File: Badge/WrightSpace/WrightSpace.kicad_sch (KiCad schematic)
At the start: 28 parts, among them J1 Conn_01x02, J2 Conn_01x02, J3 10118193-0001LF, J4 Conn_02x03_Counter_Clockwise, J5 Conn_02x03_Counter_Clockwise, J6 Conn_02x03_Counter_Clockwise, Q1 BC817, Q2 BC817, SW1 SW_SPDT, SW2 SW_SPDT, SW3 SW_SPDT, SW4 SW_SPDT, U1 ESP32-S2-SOLO, U2 HT75xx-1-SOT89

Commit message: an evenings updates
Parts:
- removed J1, J2: Conn_01x02, aerospace_badge:motor_connector, symbol Connector_Generic:Conn_01x02
- removed Q1, Q2: BC817, Package_TO_SOT_SMD:SOT-23, symbol Transistor_BJT:BC817
- removed R1: 1K, Resistor_SMD:R_0805_2012Metric_Pad1.20x1.40mm_HandSolder, symbol Device:R
- removed SW2, SW3: SW_SPDT, aerospace_badge:switch_JS202011SCQN, symbol Switch:SW_SPDT
- added D2, D3, D4, D5, D6: LED, LED_SMD:LED_1206_3216Metric_ReverseMount_Hole1.8x2.4mm, symbol Device:LED
- added R6, R7: 330, Resistor_SMD:R_0805_2012Metric_Pad1.20x1.40mm_HandSolder, symbol Device:R
- C2: value 1uF -> 100pF
- C3: value 10uF -> 1uF
- D1: footprint sunled:XZDGK45WT-9 -> LED_SMD:LED_1206_3216Metric_ReverseMount_Hole1.8x2.4mm
- R3, R4, R5: value 1K -> 330
- renumbered J5 to J1, J6 to J2, R2 to R1, R8 to R10, R9 to R2, R6 to R8, R7 to R9, SW4 to SW2
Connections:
- net Boot_Button: now also J4.5 (Pin_5); no longer J4.6 (Pin_6)
- net EN: now also J4.6 (Pin_6); no longer J4.5 (Pin_5)
- net GND: now also R3.2, R4.2, R5.2, R6.2, R7.2
- net VBUS: no longer R3.1, R4.2
- net at R5.1: now also D4.1 (K)
- net at R4.1: now also D3.1 (K)
- net LED6: now reaches U1.10 (GPIO17/U1TXD/ADC2_CH6/DAC_1)
- net LED6: now also D6.2 (A)
- net LED2: now reaches U1.21 (GPIO13/TOUCH13/ADC2_CH2/FSPIQ/FSPIIO7)
- net LED2: now also D2.2 (A)
- net LED3: now reaches U1.22 (GPIO14/TOUCH14/ADC2_CH3/FSPIWP/FSPIDQS)
- net LED3: now also D3.2 (A)
- net LED4: now reaches U1.8 (GPIO15/U0RTS/ADC2_CH4/XTAL_32K_P)
- net LED4: now also D4.2 (A)
- net LED5: now reaches U1.9 (GPIO16/U0CTS/ADC2_CH5/XTAL_32K_N)
- net LED5: now also D5.2 (A)
- net MOTOR_CTRL_MCU: no longer names the net of U1.16 (GPIO46)
- net MOTOR_CTRL_MCU_BACKUP: no longer names the net of U1.35 (MTMS/GPIO42)
- new net: D5.1 (K), R6.1
- new net: D2.1 (K), R3.1
- new net: D6.1 (K), R7.1
- no-connect marks 24 -> 21
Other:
- note added: "Programming Interface"
- note added: "The Reset (Enable) and Boot Buttons can be externalized to simplify fabrication. This will then require a rig to be assembled for programming purposes."
- note removed: "Boot Button"
- note removed: "MCU or Override Switch WiFi Controlled"
- note removed: "Manual Rotor Power Switch"
- note removed: "Motor Control"
- note removed: "Programming Connection"
- note removed: "Reset Button"
- note removed: "This needs to be here to ensure the propellers aren't spinner full speed while in backup mode. Alternatively, the other side of the backup switch could serve to go full speed/unregulated."
- moved on the sheet: D1, J1, J2, R1, R2, SW1

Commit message: weekend updates to Wright Stuff
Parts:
- removed J3: 10118193-0001LF, 10118193-0001LF:AMPHENOL_10118193-0001LF, symbol 10118193-0001LF:10118193-0001LF
- removed U2: HT75xx-1-SOT89, Package_TO_SOT_SMD:SOT-89-3, symbol Regulator_Linear:HT75xx-1-SOT89
- added C4, C5: 10uF, symbol Device:C
- added D7, D8: SunLED_RGB_ReverseMount, LED_SMD:LED_Kingbright_APFA3010_3x1.5mm_Horizontal, symbol LED:SunLED_RGB_ReverseMount
- added J2: ~, Badge_Libraries:Wright X2, symbol WrightStuff:WrightStuff
- added R1, R10, R11, R2: 30, symbol Device:R
- added R12, R13: 150, symbol Device:R
- added U2: ~, Package_TO_SOT_SMD:SOT-89-5, symbol av_Badge2023:R1170H331B-T1-FE
- J1: renamed from J4; footprint Connector_PinSocket_2.54mm:PinSocket_2x03_P2.54mm_Vertical -> aerospace_badge:esp32_programming_connector
- J3: renamed from J1; footprint Connector_PinSocket_2.54mm:PinSocket_2x03_P2.54mm_Vertical -> aerospace_badge:sao_1.69
- J4: renamed from J2; footprint Connector_PinSocket_2.54mm:PinSocket_2x03_P2.54mm_Vertical -> aerospace_badge:sao_1.69
- renumbered R9 to R14, R10 to R15, R8 to R16, R1 to R3, R2 to R4, R3 to R5, R4 to R6, R5 to R7, R6 to R8, R7 to R9
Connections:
- net VUSB is gone; now on net VBUS: SW2.1 (A)
- net EN: now also R16.1; no longer R16.2
- net GND: now also C4.1, C5.2, U2.2 (GND)
- net LED1: now also U1.13 (GPIO19/U1RTS/ADC2_CH8/CLK_OUT2/USB_D-); no longer U1.20 (GPIO12/TOUCH12/ADC2_CH1/FSPICLK/FSPIIO6)
- net LED2: now also U1.14 (GPIO20/U1CTS/ADC2_CH9/CLK_OUT1/USB_D+); no longer U1.21 (GPIO13/TOUCH13/ADC2_CH2/FSPIQ/FSPIIO7)
- net LED3: now also U1.23 (GPIO21); no longer U1.22 (GPIO14/TOUCH14/ADC2_CH3/FSPIWP/FSPIDQS)
- net LED4: now also U1.24 (SPIIO4/GPIO33/FSPIHD); no longer U1.8 (GPIO15/U0RTS/ADC2_CH4/XTAL_32K_P)
- net LED5: now also U1.25 (SPIIO5/GPIO34/FSPICS0); no longer U1.9 (GPIO16/U0CTS/ADC2_CH5/XTAL_32K_N)
- net LED6: now also U1.28 (SPIIO6/GPIO35/FSPID); no longer U1.10 (GPIO17/U1TXD/ADC2_CH6/DAC_1)
- net VBUS: now also BT1.1 (+), C4.2, U2.4 (Vin); no longer SW2.2 (B)
- net VDD33: now also R16.2, C5.1, D7.2 (A), D8.2 (A), U2.5 (Vout); no longer R16.1
- net WiFi_On/Off: now also R3.2, U1.11 (GPIO18/U1RXD/ADC2_CH7/DAC_2/CLK_OUT3); no longer U1.26 (GPIO45)
- net at SW2.3 (C): no longer BT1.1 (+)
- net at SW1.1 (A): no longer R3.2
- net TX: now reaches J1.1 (Pin_1), U1.37 (U0TXD/GPIO43/CLK_OUT1)
- net RX: now reaches J1.2 (Pin_2), U1.36 (U0RXD/GPIO44/CLK_OUT2)
- net Touch3: now reaches U1.15 (GPIO3/TOUCH3/ADC1_CH2)
- net Touch3: now also J2.3 (Touch3)
- net Touch2: now reaches U1.38 (GPIO2/TOUCH2/ADC1_CH1)
- net Touch2: now also J2.2 (Touch2)
- net Touch1: now reaches U1.39 (GPIO1/TOUCH1/ADC1_CH0)
- net Touch1: now also J2.1 (Touch1)
- net Touch4: now reaches U1.4 (GPIO4/TOUCH4/ADC1_CH3)
- net Touch4: now also J2.4 (Touch4)
- net Touch5: now reaches U1.5 (GPIO5/TOUCH5/ADC1_CH4)
- net Touch5: now also J2.5 (Touch5)
- net Touch6: now reaches U1.6 (GPIO6/TOUCH6/ADC1_CH5)
- net Touch6: now also J2.6 (Touch6)
- new net: D8.3 (G), R11.2
- new net: D8.4 (B), R2.2
- new net: SW2.2 (B), U2.1 (CE)
- new net: D7.3 (G), R10.2
- new net: D7.1 (R), R12.2
- new net: D7.4 (B), R1.2
- new net: D8.1 (R), R13.2
- new net LED1_B: R1.1, U1.22 (GPIO14/TOUCH14/ADC2_CH3/FSPIWP/FSPIDQS)
- new net LED1_G: R10.1, U1.21 (GPIO13/TOUCH13/ADC2_CH2/FSPIQ/FSPIIO7)
- new net LED1_R: R12.1, U1.20 (GPIO12/TOUCH12/ADC2_CH1/FSPICLK/FSPIIO6)
- new net LED2_B: R2.1, U1.10 (GPIO17/U1TXD/ADC2_CH6/DAC_1)
- new net LED2_G: R11.1, U1.9 (GPIO16/U0CTS/ADC2_CH5/XTAL_32K_N)
- new net LED2_R: R13.1, U1.8 (GPIO15/U0RTS/ADC2_CH4/XTAL_32K_P)
- no-connect marks 21 -> 13
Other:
- note added: "3 AAA Batteries Nominal 4.5V decaying"
- note added: "Touch Points"
- note added: "WiFi On/Off Switch"
- note removed: "GND"
- note removed: "RX"
- note removed: "TX"
- note removed: "WiFi Switch"
- title: 2023 Badge for AV Def Con -> Wright Stuff 
- moved on the sheet: BT1, C1, D1, D2, D3, D4, D5, D6, J1, J3, J4, R14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

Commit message: updated schematics
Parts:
- C1, C3: MPN (none) -> CL21B105KAFNNNE
- C2: value 100pF -> 10uF; MPN (none) -> TCP0J106M8R
- C4, C5: footprint (none) -> Capacitor_SMD:C_0805_2012Metric_Pad1.18x1.45mm_HandSolder; MPN (none) -> TCP0J106M8R
- D7, D8: MPN (none) -> XZMDKCBDDG45S-9
- R1, R10, R11, R2: footprint (none) -> Resistor_SMD:R_0805_2012Metric; MPN (none) -> RC0805FR-0730RL
- R12, R13: footprint (none) -> Resistor_SMD:R_0805_2012Metric; MPN (none) -> RC0805JR-07150RL
- U1: MPN (none) -> ESP32-S2-SOLO-2-N4
- U2: MPN (none) -> R1170H331B-T1-FE
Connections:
- net GND: now also C5.1; no longer C5.2
- net VDD33: now also C5.2; no longer C5.1
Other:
- note added: "Touch Ideas (all silver): - Ropp Signature - Small Circle on Back of Satellite - Small Circle on lower part of Satellite - Satellite Dish outer - Satellite Dish Inner"

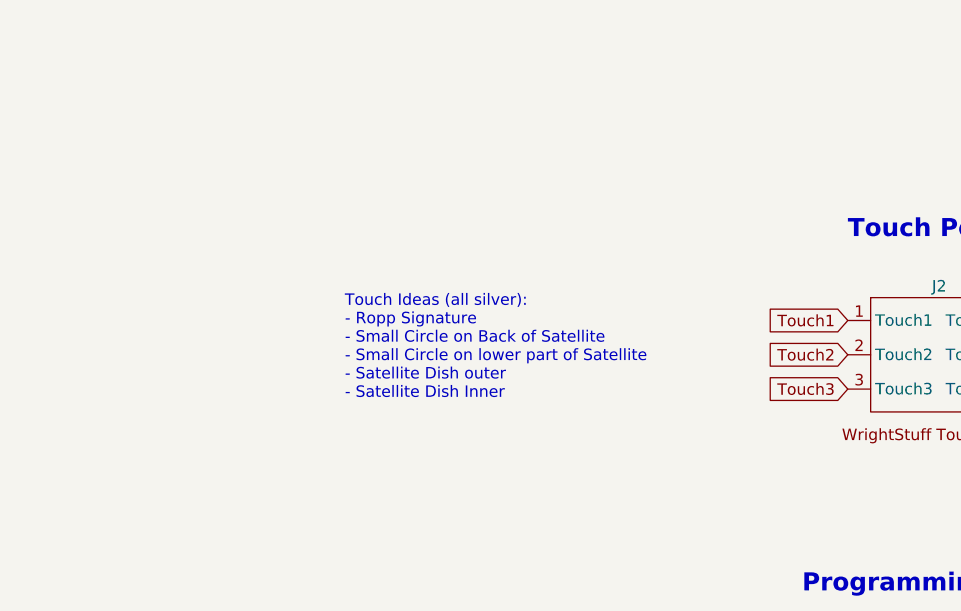
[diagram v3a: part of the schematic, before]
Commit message: updated footprint for linear voltage regulator on both badges
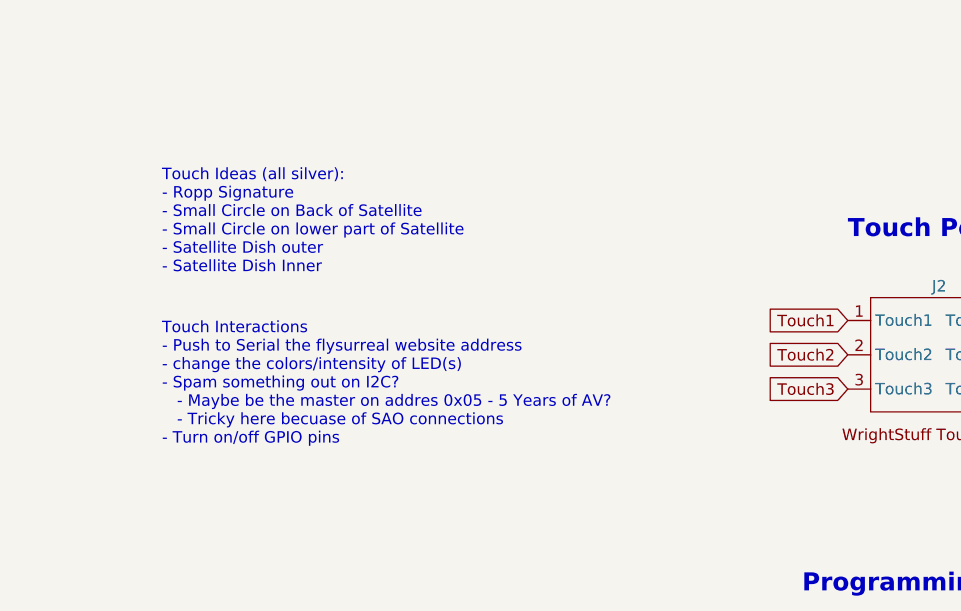
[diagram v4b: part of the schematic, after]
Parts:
- U2: footprint Package_TO_SOT_SMD:SOT-89-5 -> aerospace_badge:R1170X-SOT-89-5
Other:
- note added: "Touch Interactions - Push to Serial the flysurreal website address - change the colors/intensity of LED(s) - Spam something out on I2C? - Maybe be the master on addres 0x05 - 5 Years of AV? - Tricky here becuase of SAO connections - Turn on/off GPIO pins"
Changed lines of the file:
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@@
     (effects (font (size 2 2) (thickness 0.4) bold) (justify left bottom))
+  )
+  (text "Touch Interactions\n- Push to Serial the flysurreal website address\n- change the colors/intensity of LED(s)\n- Spam something out on I2C?\n   - Maybe be the master on addres 0x05 - 5 Years of AV?\n   - Tricky here becuase of SAO connections\n- Turn on/off GPIO pins\n"
+    (at 304.8 139.7 0)
+    (effects (font (size 1.27 1.27)) (justify left bottom))
   )
   (text "3 AAA Batteries\nNominal 4.5V decaying" (at 304.8 49.53 0)
@@
   )
   (text "Touch Ideas (all silver):\n- Ropp Signature\n- Small Circle on Back of Satellite\n- Small Circle on lower part of Satellite\n- Satellite Dish outer\n- Satellite Dish Inner"
-    (at 325.12 134.62 0)
+    (at 304.8 120.65 0)
     (effects (font (size 1.27 1.27)) (justify left bottom))
   )
@@
       (effects (font (size 1.27 1.27)))
     )
-    (property "Footprint" "Package_TO_SOT_SMD:SOT-89-5" (at 356.87 38.1 0)
-      (effects (font (size 1.27 1.27)) hide)
-    )
+    (property "Footprint" "aerospace_badge:R1170X-SOT-89-5" (at 356.87 38.1 0)
+      (effects (font (size 1.27 1.27)) hide)
+    )

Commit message: refined artwork and poc WrightStuff
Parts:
- removed J3, J4: Conn_02x03_Counter_Clockwise, aerospace_badge:sao_1.69, symbol Connector_Generic:Conn_02x03_Counter_Clockwise
- added J3, J4: ~, aerospace_badge:sao_1.69, symbol av_Badge2023:SAO_v1.69
- J2: footprint Badge_Libraries:Wright X2 -> Badge_Libraries:Wright X3
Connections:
- net GND: now also J3.2 (GND), J4.2 (GND)
- net GPIO1: now also J3.5 (GPIO1), J4.5 (GPIO1)
- net GPIO2: now also J3.6 (GPIO2), J4.6 (GPIO2)
- net SCL: now also J3.4 (SCL), J4.4 (SCL)
- net SDA: now also J3.3 (SDA), J4.3 (SDA)
- net VDD33: now also J3.1 (Vcc), J4.1 (Vcc)

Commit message: artwork tweaks to get more into KiCad
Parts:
- D1, D2, D3, D4, D5, D6: footprint LED_SMD:LED_1206_3216Metric_ReverseMount_Hole1.8x2.4mm -> aerospace_badge:led_in-s124ar; MPN (none) -> IN-S124ARUW
- D7, D8: footprint LED_SMD:LED_Kingbright_APFA3010_3x1.5mm_Horizontal -> sunled:XZMDKCBDDG45S-9

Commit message: updates, prior to fabrication
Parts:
- removed D8: SunLED_RGB_ReverseMount, sunled:XZMDKCBDDG45S-9, symbol LED:SunLED_RGB_ReverseMount
- removed J4: ~, aerospace_badge:sao_1.69, symbol av_Badge2023:SAO_v1.69
- added D1, D2, D4, D5: SunLED_RGB_ReverseMount, sunled:XZMDKCBDDG45S-9, symbol LED:SunLED_RGB_ReverseMount
- added R1, R10, R4, R5, R7, R8: 30, Resistor_SMD:R_0805_2012Metric, symbol Device:R
- added R12, R15, R16: 150, Resistor_SMD:R_0805_2012Metric, symbol Device:R
- renumbered D5 to D10, D6 to D11, D7 to D3, D1 to D6, D2 to D7, D3 to D8, D4 to D9, R12 to R14, R4 to R17, R5 to R18, R6 to R19, R7 to R20, R8 to R21, R9 to R22, R14 to R23, R15 to R24, R16 to R25, R1 to R3, R3 to R6, R10 to R9
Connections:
- net GND: now also C2.1, C3.1; no longer C2.2, C3.2
- net LED1_B: now also R2.1, R1.1; no longer R3.1
- net LED1_G: now also R7.1, R8.1; no longer R9.1
- net LED1_R: now also R13.1, R12.1; no longer R14.1
- net LED2_B: now also R3.1, R4.1, R5.1; no longer R2.1
- net LED2_G: now also R9.1, R10.1
- net LED2_R: now also R14.1, R15.1, R16.1; no longer R13.1
- net VDD33: now also C2.2, C3.2, D1.2 (A), D2.2 (A), D4.2 (A), D5.2 (A); no longer C2.1, C3.1
- net at R2.2: now also D2.4 (B)
- net at R13.2: now also D2.1 (R)
- net at R11.2: now also D5.3 (G)
- net Touch6: no longer names the net of J2.6 (Touch6)
- net Touch6: no longer U1.6 (GPIO6/TOUCH6/ADC1_CH5)
- new net: D1.3 (G), R7.2
- new net: D4.3 (G), R10.2
- new net: D2.3 (G), R8.2
- new net: D5.1 (R), R16.2
- new net: D1.4 (B), R1.2
- new net: D1.1 (R), R12.2
- new net: D4.1 (R), R15.2
- new net: D4.4 (B), R4.2
- new net: D5.4 (B), R5.2
- no-connect marks 13 -> 15
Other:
- note added: "SAO Port"
- note removed: "SAO Ports"
- moved on the sheet: D10, D11, D3, D6, D7, D8, D9, R14, R17, R18, R19, R20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

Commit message: inclusion of defcon logo
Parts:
- SW1, SW2: MPN (none) -> JS202011SCQN
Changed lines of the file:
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@@
       (effects (font (size 1.27 1.27)) hide)
     )
-    (property "Datasheet" "~" (at 342.9 38.1 0)
+    (property "Datasheet" "https://www.ckswitches.com/media/1422/js.pdf" (at 342.9 38.1 0)
+      (effects (font (size 1.27 1.27)) hide)
+    )
+    (property "MPN" "JS202011SCQN" (at 342.9 38.1 0)
       (effects (font (size 1.27 1.27)) hide)
     )
@@
       (effects (font (size 1.27 1.27)) hide)
     )
-    (property "Datasheet" "~" (at 50.8 54.61 0)
+    (property "Datasheet" "https://www.ckswitches.com/media/1422/js.pdf" (at 50.8 54.61 0)
       (effects (font (size 1.27 1.27)) hide)
     )
+    (property "MPN" "JS202011SCQN" (at 50.8 54.61 0)
+      (effects (font (size 1.27 1.27)) hide)
+    )
